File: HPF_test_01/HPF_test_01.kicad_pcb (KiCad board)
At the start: 2 copper layers, 68.8 x 29.2 mm, 12 parts, among them T1 GT07-110-013

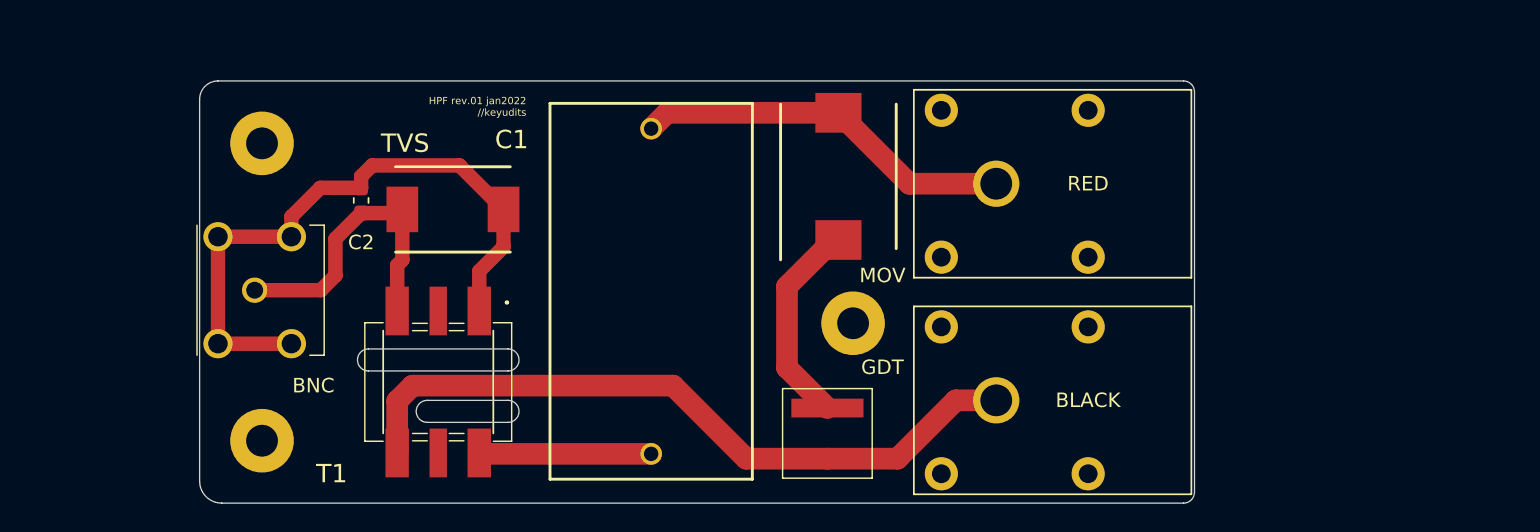
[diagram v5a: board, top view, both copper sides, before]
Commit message: Turned C1 on its side to save space, updated footprint & board size, updated enclosure.
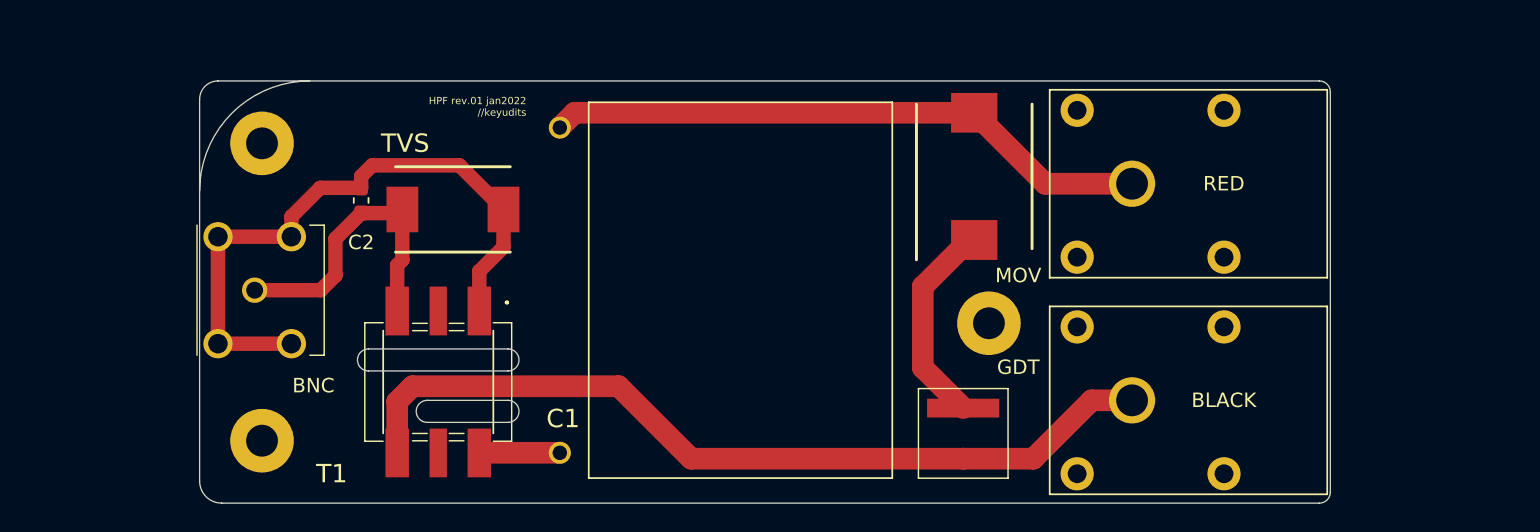
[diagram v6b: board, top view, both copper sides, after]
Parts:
- C1: footprint ECQ-UBAF4747K_kicad:ECQUBAF474K -> ECQ-UBAF4747K_kicad:ECQ-UBAF474K-3_side
- moved C1 12.0 mm to (123.2, 88.9), turned to 180 degrees
- moved BLACK 9.40 mm to (160.8, 96.5)
- moved GDT 9.40 mm to (149.1, 98.8)
- moved MOV 9.40 mm to (149.9, 81.0)
- moved RED 9.40 mm to (160.8, 81.5)
- moved REF** 9.40 mm to (150.9, 91.2)
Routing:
- net Net-(C1-Pad1): track 26.4 -> 42.0 mm
- net Net-(J2_BLACK1-Pad1): track 49.2 -> 58.6 mm
- net Net-(C1-Pad2): track 11.9 -> 5.58 mm
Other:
- board size 68.8 x 29.2 mm -> 78.2 x 29.2 mm

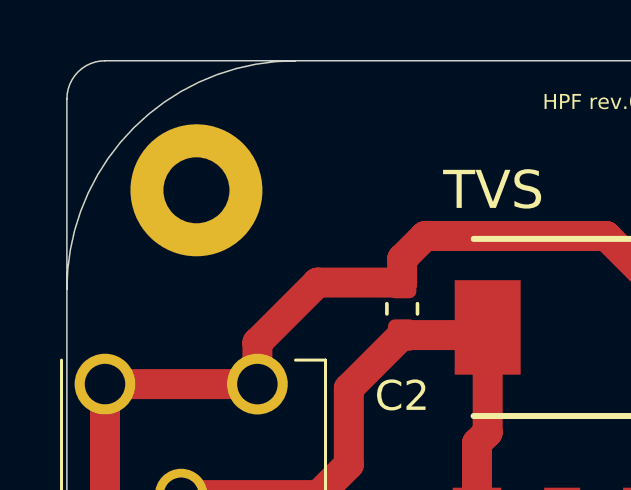
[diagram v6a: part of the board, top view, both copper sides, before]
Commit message: Added first .stl file and feb3 render png's
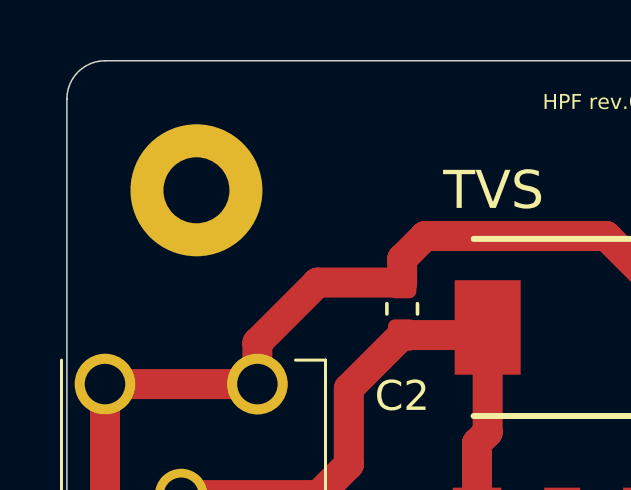
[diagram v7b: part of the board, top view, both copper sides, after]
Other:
- outline, holes or cut-outs redrawn
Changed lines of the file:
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@@
   (general
     (thickness 1.6)
-    (drawings 20)
+    (drawings 19)
     (tracks 40)
     (zones 0)
@@
     )
   )
-  (gr_arc (start 103.886 82.042) (end 103.886 74.422) (angle -90) (layer Edge.Cuts) (width 0.05))
   (gr_text "non-plated cutout\n" (at 114.808 97.282) (layer Cmts.User)
     (effects (font (size 0.5 0.5) (thickness 0.125)))
@@
   (segment (start 97.536 92.6) (end 97.536 85.2) (width 1) (layer F.Cu) (net 4))
   (segment (start 97.536 92.6) (end 102.616 92.6) (width 1) (layer F.Cu) (net 4))
+  (segment (start 149.86 85.426) (end 149.524 85.426) (width 1.5) (layer F.Cu) (net 5))
+  (segment (start 146.304 94.262) (end 149.098 97.056) (width 1.5) (layer F.Cu) (net 5))
   (segment (start 146.304 88.646) (end 146.304 94.262) (width 1.5) (layer F.Cu) (net 5))
   (segment (start 149.524 85.426) (end 146.304 88.646) (width 1.5) (layer F.Cu) (net 5))
-  (segment (start 149.86 85.426) (end 149.524 85.426) (width 1.5) (layer F.Cu) (net 5))
-  (segment (start 146.304 94.262) (end 149.098 97.056) (width 1.5) (layer F.Cu) (net 5))
   (segment (start 149.098 100.556) (end 153.952 100.556) (width 1.5) (layer F.Cu) (net 8))
   (segment (start 157.988 96.52) (end 160.782 96.52) (width 1.5) (layer F.Cu) (net 8))

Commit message: Added Gerber files [hpf_test_01_gerber_v01]
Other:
- board text added: "JLCJLCJLCJLC"
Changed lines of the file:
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@@
   (general
     (thickness 1.6)
-    (drawings 19)
+    (drawings 20)
     (tracks 40)
     (zones 0)
@@
     (visible_elements FFFFFF7F)
     (pcbplotparams
-      (layerselection 0x010fc_ffffffff)
-      (usegerberextensions false)
-      (usegerberattributes true)
-      (usegerberadvancedattributes true)
-      (creategerberjobfile true)
+      (layerselection 0x012fc_ffffffff)
+      (usegerberextensions true)
+      (usegerberattributes false)
+      (usegerberadvancedattributes false)
+      (creategerberjobfile false)
       (excludeedgelayer true)
       (linewidth 0.100000)
@@
       (plotinvisibletext false)
       (padsonsilk false)
-      (subtractmaskfromsilk false)
+      (subtractmaskfromsilk true)
       (outputformat 1)
       (mirror false)
-      (drillshape 1)
+      (drillshape 0)
       (scaleselection 1)
-      (outputdirectory ""))
+      (outputdirectory "HPF_test_01_Gerber_v01/"))
   )
   (net 0 "")
@@
     (add_net "Net-(T1-Pad5)")
   )
-  (module ECQ-UBAF4747K_kicad:ECQ-UBAF474K-3_side (layer F.Cu)
-    (at 123.19 88.9 180)
-    (fp_text reference C1 (at 1.778 -8.89) (layer F.SilkS)
-      (effects (font (size 1.27 1.27) (thickness 0.15)))
-    )
-    (fp_text value ECQ-UBAF474K (at 10.922 0 180) (layer F.SilkS) hide
-      (effects (font (size 1.27 1.27) (thickness 0.254)))
-    )
-    (fp_line (start 0 12.954) (end 0 -12.954) (layer F.Fab) (width 0.12))
-    (fp_line (start -21.082 12.954) (end 0 12.954) (layer F.Fab) (width 0.12))
-    (fp_line (start -21.082 -12.954) (end -21.082 12.954) (layer F.Fab) (width 0.12))
-    (fp_line (start 0 -12.954) (end -21.082 -12.954) (layer F.Fab) (width 0.12))
-    (fp_line (start 0 13) (end 0 -13) (layer F.SilkS) (width 0.12))
-    (fp_line (start 0 13) (end -21 13) (layer F.SilkS) (width 0.12))
-    (fp_line (start -21 13) (end -21 -13) (layer F.SilkS) (width 0.12))
-    (fp_line (start 0 -13) (end -21 -13) (layer F.SilkS) (width 0.12))
-    (fp_line (start -21.59 -13.97) (end 3.302 -13.97) (layer F.CrtYd) (width 0.12))
-    (fp_line (start 3.302 -13.97) (end 3.302 13.97) (layer F.CrtYd) (width 0.12))
-    (fp_line (start 3.302 13.97) (end -21.59 13.97) (layer F.CrtYd) (width 0.12))
-    (fp_line (start -21.59 13.97) (end -21.59 -13.97) (layer F.CrtYd) (width 0.12))
-    (fp_text user %R (at 7.62 0 90) (layer F.Fab)
-      (effects (font (size 1.27 1.27) (thickness 0.254)))
-    )
-    (fp_text user C** (at 2.032 -0.254 270) (layer F.Fab)
-      (effects (font (size 1 1) (thickness 0.15)))
-    )
-    (pad 1 thru_hole circle (at 2 11.25 180) (size 1.524 1.524) (drill 1) (layers *.Cu *.Mask)
-      (net 2 "Net-(C1-Pad1)"))
-    (pad 2 thru_hole circle (at 2 -11.25 180) (size 1.524 1.524) (drill 1) (layers *.Cu *.Mask)
-      (net 1 "Net-(C1-Pad2)"))
-  )
   (module GT07-110-013-Modifed:GT07110013 (layer F.Cu)
     (at 112.776 95.25)
@@
     (fp_line (start 6 7.6) (end -6 7.6) (layer F.CrtYd) (width 0.1))
     (fp_line (start -6 7.6) (end -6 -7.6) (layer F.CrtYd) (width 0.1))
-    (fp_line (start 4.7 -5.5) (end 4.7 -5.5) (layer F.SilkS) (width 0.2))
-    (fp_line (start 4.8 -5.5) (end 4.8 -5.5) (layer F.SilkS) (width 0.2))
-    (fp_line (start 4.7 -5.5) (end 4.7 -5.5) (layer F.SilkS) (width 0.2))
+    (fp_line (start -4.698 5.676) (end -4.698 5.676) (layer F.SilkS) (width 0.2))
+    (fp_line (start -4.598 5.676) (end -4.598 5.676) (layer F.SilkS) (width 0.2))
+    (fp_line (start -4.698 5.676) (end -4.698 5.676) (layer F.SilkS) (width 0.2))
     (fp_text user %R (at 7.112 -5.588 90) (layer F.Fab)
       (effects (font (size 1.27 1.27) (thickness 0.254)))
     )
-    (fp_arc (start 4.75 -5.5) (end 4.7 -5.5) (angle -180) (layer F.SilkS) (width 0.2))
-    (fp_arc (start 4.75 -5.5) (end 4.8 -5.5) (angle -180) (layer F.SilkS) (width 0.2))
-    (fp_arc (start 4.75 -5.5) (end 4.7 -5.5) (angle -180) (layer F.SilkS) (width 0.2))
+    (fp_arc (start -4.648 5.676) (end -4.698 5.676) (angle -180) (layer F.SilkS) (width 0.2))
+    (fp_arc (start -4.648 5.676) (end -4.598 5.676) (angle -180) (layer F.SilkS) (width 0.2))
+    (fp_arc (start -4.648 5.676) (end -4.698 5.676) (angle -180) (layer F.SilkS) (width 0.2))
     (pad 1 smd rect (at 2.84 -4.91) (size 1.62 3.375) (layers F.Cu F.Paste F.Mask)
       (net 4 "Net-(C2-Pad1)"))
@@
       (net 6 "Net-(T1-Pad5)"))
     (pad 6 smd rect (at 2.84 4.91) (size 1.62 3.375) (layers F.Cu F.Paste F.Mask)
+      (net 1 "Net-(C1-Pad2)"))
+  )
+  (module ECQ-UBAF4747K_kicad:ECQ-UBAF474K-3_side (layer F.Cu)
+    (at 123.19 88.9 180)
+    (fp_text reference C1 (at 1.778 -8.89) (layer F.SilkS)
+      (effects (font (size 1.27 1.27) (thickness 0.15)))
+    )
+    (fp_text value ECQ-UBAF474K (at 10.922 0 180) (layer F.SilkS) hide
+      (effects (font (size 1.27 1.27) (thickness 0.254)))
+    )
+    (fp_line (start 0 12.954) (end 0 -12.954) (layer F.Fab) (width 0.12))
+    (fp_line (start -21.082 12.954) (end 0 12.954) (layer F.Fab) (width 0.12))
+    (fp_line (start -21.082 -12.954) (end -21.082 12.954) (layer F.Fab) (width 0.12))
+    (fp_line (start 0 -12.954) (end -21.082 -12.954) (layer F.Fab) (width 0.12))
+    (fp_line (start 0 13) (end 0 -13) (layer F.SilkS) (width 0.12))
+    (fp_line (start 0 13) (end -21 13) (layer F.SilkS) (width 0.12))
+    (fp_line (start -21 13) (end -21 -13) (layer F.SilkS) (width 0.12))
+    (fp_line (start 0 -13) (end -21 -13) (layer F.SilkS) (width 0.12))
+    (fp_line (start -21.59 -13.97) (end 3.302 -13.97) (layer F.CrtYd) (width 0.12))
+    (fp_line (start 3.302 -13.97) (end 3.302 13.97) (layer F.CrtYd) (width 0.12))
+    (fp_line (start 3.302 13.97) (end -21.59 13.97) (layer F.CrtYd) (width 0.12))
+    (fp_line (start -21.59 13.97) (end -21.59 -13.97) (layer F.CrtYd) (width 0.12))
+    (fp_text user %R (at 7.62 0 90) (layer F.Fab)
+      (effects (font (size 1.27 1.27) (thickness 0.254)))
+    )
+    (fp_text user C** (at 2.032 -0.254 270) (layer F.Fab)
+      (effects (font (size 1 1) (thickness 0.15)))
+    )
+    (pad 1 thru_hole circle (at 2 11.25 180) (size 1.524 1.524) (drill 1) (layers *.Cu *.Mask)
+      (net 2 "Net-(C1-Pad1)"))
+    (pad 2 thru_hole circle (at 2 -11.25 180) (size 1.524 1.524) (drill 1) (layers *.Cu *.Mask)
       (net 1 "Net-(C1-Pad2)"))
   )
@@
     )
   )
+  (gr_text JLCJLCJLCJLC (at 135.128 101.346) (layer B.SilkS)
+    (effects (font (size 1 1) (thickness 0.15)) (justify mirror))
+  )
   (gr_text "non-plated cutout\n" (at 114.808 97.282) (layer Cmts.User)
